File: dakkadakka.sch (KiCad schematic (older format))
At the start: 75 parts

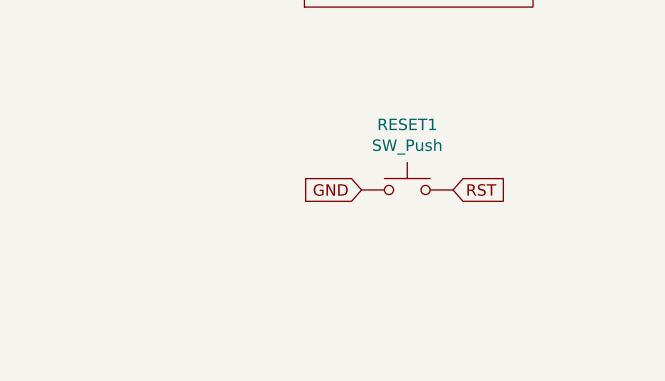
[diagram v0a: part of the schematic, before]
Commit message: Reversible PCB update
Reversible PCB update
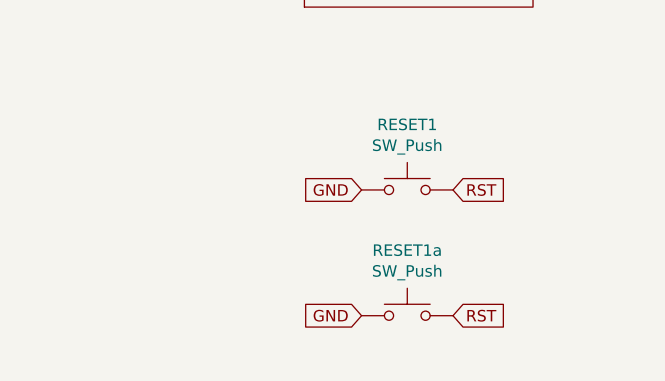
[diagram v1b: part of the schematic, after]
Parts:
- added RESET1a: SW_Push, Button_Switch_SMD:SW_SPST_SKQG_WithoutStem, symbol Switch:SW_Push
- D1, D10, D11, D12, D13, D14, D15, D16, D17, D18, D19, D2, D20, D21, D22, D23, D24, D25, D26, D27, D28, D29, D3, D30, D31, D32, D33, D34, D35, D36, D4, D5, D6, D7, D8, D9: footprint Keebio-Parts:Diode-Hybrid-Back -> Keebio-Parts:Diode-dual
- MX1, MX10, MX11, MX12, MX13, MX14, MX15, MX16, MX17, MX18, MX19, MX2, MX20, MX21, MX22, MX23, MX24, MX25, MX26, MX27, MX28, MX29, MX3, MX30, MX31, MX32, MX33, MX34, MX35, MX36, MX4, MX5, MX6, MX7, MX8, MX9: footprint MX_Only:MXOnly-1U-NoLED -> MX_Only:MX_ONLY_1u_NOLED_REVERSIBLE
- MX30a1: footprint MX_Only:MXOnly-2U-ReversedStabilizers-NoLED -> MX_Only:MXOnly-2U-NoLED-REVERSIBLE
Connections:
- net GND: now also RESET1a.1
- net RST: now also RESET1a.2
